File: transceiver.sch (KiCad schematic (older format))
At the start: 44 parts, among them U3 CC1200, Y1 40 Mhz crystal

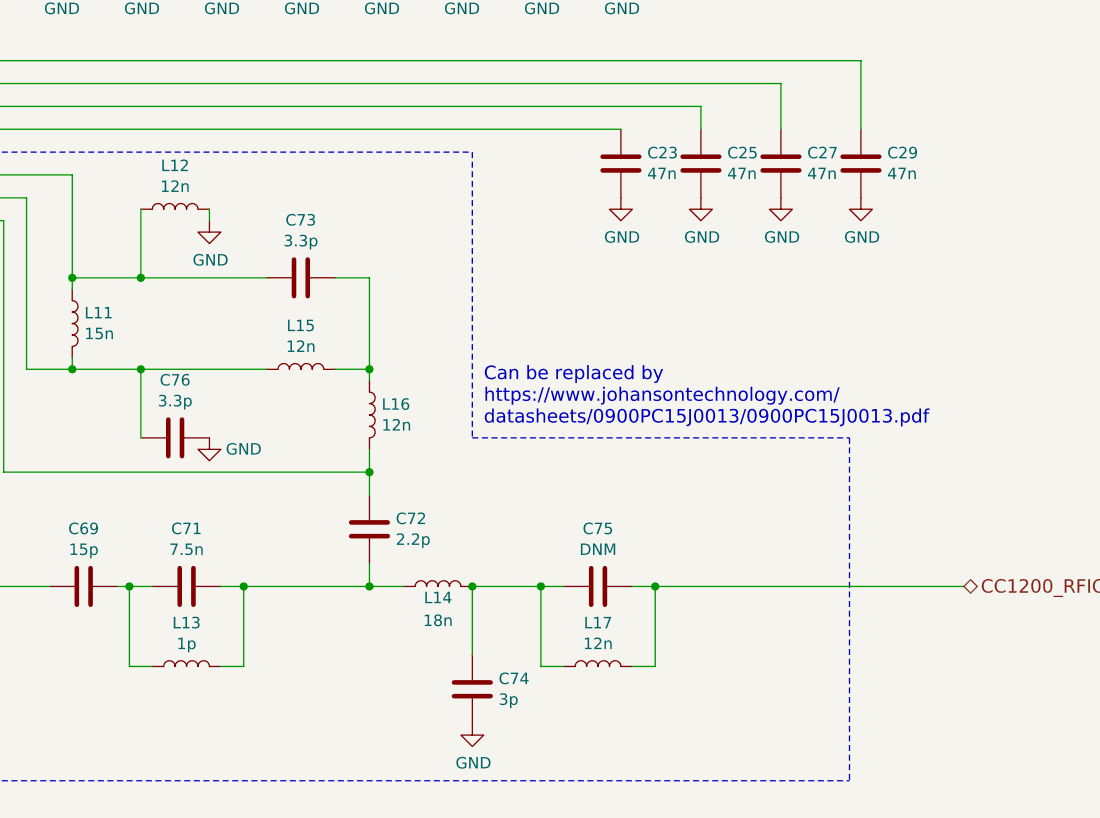
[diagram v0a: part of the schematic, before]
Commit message: Corrected some component values
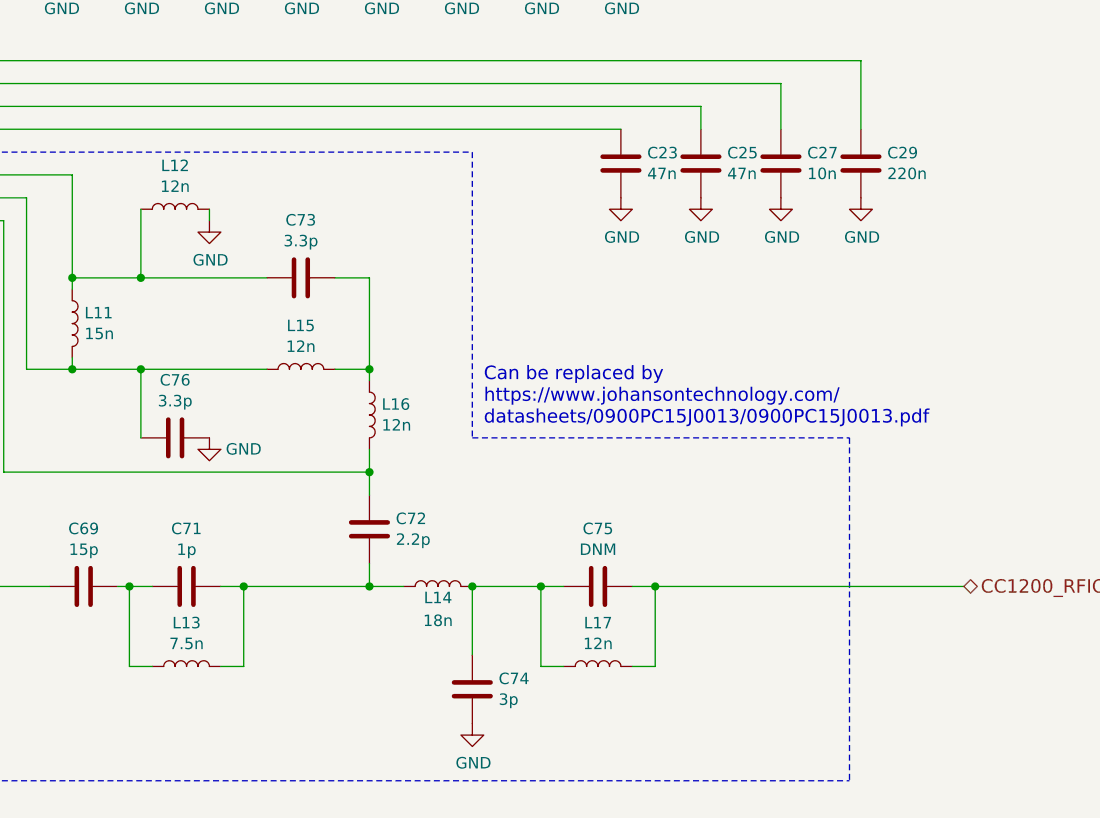
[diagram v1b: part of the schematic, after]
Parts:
- C27: value 47n -> 10n
- C29: value 47n -> 220n
- C71: value 7.5n -> 1p
- L13: value 1p -> 7.5n
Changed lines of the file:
@@
 P 6600 5300
 F 0 "C71" V 6348 5300 50  0000 C CNN
-F 1 "7.5n" V 6439 5300 50  0000 C CNN
+F 1 "1p" V 6439 5300 50  0000 C CNN
 F 2 "" H 6638 5150 50  0001 C CNN
 F 3 "~" H 6600 5300 50  0001 C CNN
@@
 P 6600 5650
 F 0 "L13" V 6790 5650 50  0000 C CNN
-F 1 "1p" V 6699 5650 50  0000 C CNN
+F 1 "7.5n" V 6699 5650 50  0000 C CNN
 F 2 "" H 6600 5650 50  0001 C CNN
 F 3 "~" H 6600 5650 50  0001 C CNN
@@
 P 9200 3450
 F 0 "C27" H 9315 3496 50  0000 L CNN
-F 1 "47n" H 9315 3405 50  0000 L CNN
+F 1 "10n" H 9315 3405 50  0000 L CNN
 F 2 "" H 9238 3300 50  0001 C CNN
 F 3 "~" H 9200 3450 50  0001 C CNN
@@
 P 9550 3450
 F 0 "C29" H 9665 3496 50  0000 L CNN
-F 1 "47n" H 9665 3405 50  0000 L CNN
+F 1 "220n" H 9665 3405 50  0000 L CNN
 F 2 "" H 9588 3300 50  0001 C CNN
 F 3 "~" H 9550 3450 50  0001 C CNN

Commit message: Added MCU config pins
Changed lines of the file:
@@
 $Descr A4 11693 8268
 encoding utf-8
-Sheet 6 6
+Sheet 5 6
 Title ""
 Date ""
@@
 Wire Wire Line
 	1750 2900 2400 2900
-Wire Wire Line
-	5400 2000 5400 1900
 $Comp
 L Device:C C60
@@
 Wire Wire Line
 	5550 5100 5550 5300
+Wire Wire Line
+	5400 1900 5400 2000
 $EndSCHEMATC

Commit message: Changes to PA layout
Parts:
- C19, C20, C21, C22, C23, C24, C25, C26, C27, C28, C29, C30, C31, C32, C57, C58, C59, C60, C61, C62, C66, C67, C68, C69, C71, C72, C73, C74, C75, C76: footprint (none) -> Capacitor_SMD:C_0603_1608Metric
- L10, L11, L12, L13, L14, L15, L16, L17: footprint (none) -> Inductor_SMD:L_0603_1608Metric
- R13, R6: footprint (none) -> Resistor_SMD:R_0603_1608Metric
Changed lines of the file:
@@
 $Descr A4 11693 8268
 encoding utf-8
-Sheet 5 6
+Sheet 4 6
 Title ""
 Date ""
@@
 F 0 "C23" H 8615 3496 50  0000 L CNN
 F 1 "47n" H 8615 3405 50  0000 L CNN
-F 2 "" H 8538 3300 50  0001 C CNN
+F 2 "Capacitor_SMD:C_0603_1608Metric" H 8538 3300 50  0001 C CNN
 F 3 "~" H 8500 3450 50  0001 C CNN
 	1    8500 3450
@@
 F 0 "R6" H 3080 3604 50  0000 R CNN
 F 1 "56k" H 3080 3695 50  0000 R CNN
-F 2 "" V 3080 3650 50  0001 C CNN
+F 2 "Resistor_SMD:R_0603_1608Metric" V 3080 3650 50  0001 C CNN
 F 3 "~" H 3150 3650 50  0001 C CNN
 	1    3150 3650
@@
 F 0 "C59" H 2915 3696 50  0000 L CNN
 F 1 "DNM" H 2915 3605 50  0000 L CNN
-F 2 "" H 2838 3500 50  0001 C CNN
+F 2 "Capacitor_SMD:C_0603_1608Metric" H 2838 3500 50  0001 C CNN
 F 3 "~" H 2800 3650 50  0001 C CNN
 	1    2800 3650
@@
 F 0 "C58" H 2515 3696 50  0000 L CNN
 F 1 "15p" H 2515 3605 50  0000 L CNN
-F 2 "" H 2438 3500 50  0001 C CNN
+F 2 "Capacitor_SMD:C_0603_1608Metric" H 2438 3500 50  0001 C CNN
 F 3 "~" H 2400 3650 50  0001 C CNN
 	1    2400 3650
@@
 F 0 "C57" H 2115 3696 50  0000 L CNN
 F 1 "15p" H 2115 3605 50  0000 L CNN
-F 2 "" H 2038 3500 50  0001 C CNN
+F 2 "Capacitor_SMD:C_0603_1608Metric" H 2038 3500 50  0001 C CNN
 F 3 "~" H 2000 3650 50  0001 C CNN
 	1    2000 3650
@@
 F 0 "C60" H 2165 1446 50  0000 L CNN
 F 1 "100n" H 2165 1355 50  0000 L CNN
-F 2 "" H 2088 1250 50  0001 C CNN
+F 2 "Capacitor_SMD:C_0603_1608Metric" H 2088 1250 50  0001 C CNN
 F 3 "~" H 2050 1400 50  0001 C CNN
 	1    2050 1400
@@
 F 0 "C62" H 3865 1446 50  0000 L CNN
 F 1 "2.2u" H 3865 1355 50  0000 L CNN
-F 2 "" H 3788 1250 50  0001 C CNN
+F 2 "Capacitor_SMD:C_0603_1608Metric" H 3788 1250 50  0001 C CNN
 F 3 "~" H 3750 1400 50  0001 C CNN
 	1    3750 1400
@@
 F 0 "R13" H 5220 5346 50  0000 L CNN
 F 1 "10" H 5220 5255 50  0000 L CNN
-F 2 "" V 5080 5300 50  0001 C CNN
+F 2 "Resistor_SMD:R_0603_1608Metric" V 5080 5300 50  0001 C CNN
 F 3 "~" H 5150 5300 50  0001 C CNN
 	1    5150 5300
@@
 F 0 "C67" H 4915 5346 50  0000 L CNN
 F 1 "33p" H 4915 5255 50  0000 L CNN
-F 2 "" H 4838 5150 50  0001 C CNN
+F 2 "Capacitor_SMD:C_0603_1608Metric" H 4838 5150 50  0001 C CNN
 F 3 "~" H 4800 5300 50  0001 C CNN
 	1    4800 5300
@@
 F 0 "C66" H 5265 5796 50  0000 L CNN
 F 1 "10n" H 5265 5705 50  0000 L CNN
-F 2 "" H 5188 5600 50  0001 C CNN
+F 2 "Capacitor_SMD:C_0603_1608Metric" H 5188 5600 50  0001 C CNN
 F 3 "~" H 5150 5750 50  0001 C CNN
 	1    5150 5750
@@
 F 0 "C68" H 4915 5796 50  0000 L CNN
 F 1 "100p" H 4915 5705 50  0000 L CNN
-F 2 "" H 4838 5600 50  0001 C CNN
+F 2 "Capacitor_SMD:C_0603_1608Metric" H 4838 5600 50  0001 C CNN
 F 3 "~" H 4800 5750 50  0001 C CNN
 	1    4800 5750
@@
 F 0 "C69" V 5898 5300 50  0000 C CNN
 F 1 "15p" V 5989 5300 50  0000 C CNN
-F 2 "" H 6188 5150 50  0001 C CNN
+F 2 "Capacitor_SMD:C_0603_1608Metric" H 6188 5150 50  0001 C CNN
 F 3 "~" H 6150 5300 50  0001 C CNN
 	1    6150 5300
@@
 F 0 "C71" V 6348 5300 50  0000 C CNN
 F 1 "1p" V 6439 5300 50  0000 C CNN
-F 2 "" H 6638 5150 50  0001 C CNN
+F 2 "Capacitor_SMD:C_0603_1608Metric" H 6638 5150 50  0001 C CNN
 F 3 "~" H 6600 5300 50  0001 C CNN
 	1    6600 5300
@@
 F 0 "L13" V 6790 5650 50  0000 C CNN
 F 1 "7.5n" V 6699 5650 50  0000 C CNN
-F 2 "" H 6600 5650 50  0001 C CNN
+F 2 "Inductor_SMD:L_0603_1608Metric" H 6600 5650 50  0001 C CNN
 F 3 "~" H 6600 5650 50  0001 C CNN
 	1    6600 5650
@@
 F 0 "C75" V 8148 5300 50  0000 C CNN
 F 1 "DNM" V 8239 5300 50  0000 C CNN
-F 2 "" H 8438 5150 50  0001 C CNN
+F 2 "Capacitor_SMD:C_0603_1608Metric" H 8438 5150 50  0001 C CNN
 F 3 "~" H 8400 5300 50  0001 C CNN
 	1    8400 5300
@@
 F 0 "L17" V 8590 5650 50  0000 C CNN
 F 1 "12n" V 8499 5650 50  0000 C CNN
-F 2 "" H 8400 5650 50  0001 C CNN
+F 2 "Inductor_SMD:L_0603_1608Metric" H 8400 5650 50  0001 C CNN
 F 3 "~" H 8400 5650 50  0001 C CNN
 	1    8400 5650
@@
 F 0 "C74" H 7965 5796 50  0000 L CNN
 F 1 "3p" H 7965 5705 50  0000 L CNN
-F 2 "" H 7888 5600 50  0001 C CNN
+F 2 "Capacitor_SMD:C_0603_1608Metric" H 7888 5600 50  0001 C CNN
 F 3 "~" H 7850 5750 50  0001 C CNN
 	1    7850 5750
@@
 F 0 "L14" V 7650 5300 50  0000 C CNN
 F 1 "18n" V 7550 5300 50  0000 C CNN
-F 2 "" H 7700 5300 50  0001 C CNN
+F 2 "Inductor_SMD:L_0603_1608Metric" H 7700 5300 50  0001 C CNN
 F 3 "~" H 7700 5300 50  0001 C CNN
 	1    7700 5300
@@
 F 0 "L15" V 7290 4350 50  0000 C CNN
 F 1 "12n" V 7199 4350 50  0000 C CNN
-F 2 "" H 7100 4350 50  0001 C CNN
+F 2 "Inductor_SMD:L_0603_1608Metric" H 7100 4350 50  0001 C CNN
 F 3 "~" H 7100 4350 50  0001 C CNN
 	1    7100 4350
@@
 F 0 "L16" H 7453 4596 50  0000 L CNN
 F 1 "12n" H 7453 4505 50  0000 L CNN
-F 2 "" H 7400 4550 50  0001 C CNN
+F 2 "Inductor_SMD:L_0603_1608Metric" H 7400 4550 50  0001 C CNN
 F 3 "~" H 7400 4550 50  0001 C CNN
 	1    7400 4550
@@
 F 0 "C73" V 6848 3950 50  0000 C CNN
 F 1 "3.3p" V 6939 3950 50  0000 C CNN
-F 2 "" H 7138 3800 50  0001 C CNN
+F 2 "Capacitor_SMD:C_0603_1608Metric" H 7138 3800 50  0001 C CNN
 F 3 "~" H 7100 3950 50  0001 C CNN
 	1    7100 3950
@@
 F 0 "L12" V 6740 3650 50  0000 C CNN
 F 1 "12n" V 6649 3650 50  0000 C CNN
-F 2 "" H 6550 3650 50  0001 C CNN
+F 2 "Inductor_SMD:L_0603_1608Metric" H 6550 3650 50  0001 C CNN
 F 3 "~" H 6550 3650 50  0001 C CNN
 	1    6550 3650
@@
 F 0 "C76" V 6298 4650 50  0000 C CNN
 F 1 "3.3p" V 6389 4650 50  0000 C CNN
-F 2 "" H 6588 4500 50  0001 C CNN
+F 2 "Capacitor_SMD:C_0603_1608Metric" H 6588 4500 50  0001 C CNN
 F 3 "~" H 6550 4650 50  0001 C CNN
 	1    6550 4650
@@
 F 0 "C72" H 7515 5096 50  0000 L CNN
 F 1 "2.2p" H 7515 5005 50  0000 L CNN
-F 2 "" H 7438 4900 50  0001 C CNN
+F 2 "Capacitor_SMD:C_0603_1608Metric" H 7438 4900 50  0001 C CNN
 F 3 "~" H 7400 5050 50  0001 C CNN
 	1    7400 5050
@@
 F 0 "L10" V 5540 5100 50  0000 C CNN
 F 1 "10n" V 5449 5100 50  0000 C CNN
-F 2 "" H 5350 5100 50  0001 C CNN
+F 2 "Inductor_SMD:L_0603_1608Metric" H 5350 5100 50  0001 C CNN
 F 3 "~" H 5350 5100 50  0001 C CNN
 	1    5350 5100
@@
 F 0 "C25" H 8965 3496 50  0000 L CNN
 F 1 "47n" H 8965 3405 50  0000 L CNN
-F 2 "" H 8888 3300 50  0001 C CNN
+F 2 "Capacitor_SMD:C_0603_1608Metric" H 8888 3300 50  0001 C CNN
 F 3 "~" H 8850 3450 50  0001 C CNN
 	1    8850 3450
@@
 F 0 "C27" H 9315 3496 50  0000 L CNN
 F 1 "10n" H 9315 3405 50  0000 L CNN
-F 2 "" H 9238 3300 50  0001 C CNN
+F 2 "Capacitor_SMD:C_0603_1608Metric" H 9238 3300 50  0001 C CNN
 F 3 "~" H 9200 3450 50  0001 C CNN
 	1    9200 3450
@@
 F 0 "C29" H 9665 3496 50  0000 L CNN
 F 1 "220n" H 9665 3405 50  0000 L CNN
-F 2 "" H 9588 3300 50  0001 C CNN
+F 2 "Capacitor_SMD:C_0603_1608Metric" H 9588 3300 50  0001 C CNN
 F 3 "~" H 9550 3450 50  0001 C CNN
 	1    9550 3450
@@
 F 0 "C20" H 5815 2496 50  0000 L CNN
 F 1 "47n" H 5815 2405 50  0000 L CNN
-F 2 "" H 5738 2300 50  0001 C CNN
+F 2 "Capacitor_SMD:C_0603_1608Metric" H 5738 2300 50  0001 C CNN
 F 3 "~" H 5700 2450 50  0001 C CNN
 	1    5700 2450
@@
 F 0 "C21" H 6165 2496 50  0000 L CNN
 F 1 "47n" H 6165 2405 50  0000 L CNN
-F 2 "" H 6088 2300 50  0001 C CNN
+F 2 "Capacitor_SMD:C_0603_1608Metric" H 6088 2300 50  0001 C CNN
 F 3 "~" H 6050 2450 50  0001 C CNN
 	1    6050 2450
@@
 F 0 "C22" H 6515 2496 50  0000 L CNN
 F 1 "47n" H 6515 2405 50  0000 L CNN
-F 2 "" H 6438 2300 50  0001 C CNN
+F 2 "Capacitor_SMD:C_0603_1608Metric" H 6438 2300 50  0001 C CNN
 F 3 "~" H 6400 2450 50  0001 C CNN
 	1    6400 2450
@@
 F 0 "C24" H 6865 2496 50  0000 L CNN
 F 1 "47n" H 6865 2405 50  0000 L CNN
-F 2 "" H 6788 2300 50  0001 C CNN
+F 2 "Capacitor_SMD:C_0603_1608Metric" H 6788 2300 50  0001 C CNN
 F 3 "~" H 6750 2450 50  0001 C CNN
 	1    6750 2450
@@
 F 0 "C26" H 7215 2496 50  0000 L CNN
 F 1 "47n" H 7215 2405 50  0000 L CNN
-F 2 "" H 7138 2300 50  0001 C CNN
+F 2 "Capacitor_SMD:C_0603_1608Metric" H 7138 2300 50  0001 C CNN
 F 3 "~" H 7100 2450 50  0001 C CNN
 	1    7100 2450
@@
 F 0 "C28" H 7565 2496 50  0000 L CNN
 F 1 "47n" H 7565 2405 50  0000 L CNN
-F 2 "" H 7488 2300 50  0001 C CNN
+F 2 "Capacitor_SMD:C_0603_1608Metric" H 7488 2300 50  0001 C CNN
 F 3 "~" H 7450 2450 50  0001 C CNN
 	1    7450 2450
@@
 F 0 "C30" H 7915 2496 50  0000 L CNN
 F 1 "47n" H 7915 2405 50  0000 L CNN
-F 2 "" H 7838 2300 50  0001 C CNN
+F 2 "Capacitor_SMD:C_0603_1608Metric" H 7838 2300 50  0001 C CNN
 F 3 "~" H 7800 2450 50  0001 C CNN
 	1    7800 2450
@@
 F 0 "C31" H 8265 2496 50  0000 L CNN
 F 1 "47n" H 8265 2405 50  0000 L CNN
-F 2 "" H 8188 2300 50  0001 C CNN
+F 2 "Capacitor_SMD:C_0603_1608Metric" H 8188 2300 50  0001 C CNN
 F 3 "~" H 8150 2450 50  0001 C CNN
 	1    8150 2450
@@
 F 0 "C32" H 8615 2496 50  0000 L CNN
 F 1 "47n" H 8615 2405 50  0000 L CNN
-F 2 "" H 8538 2300 50  0001 C CNN
+F 2 "Capacitor_SMD:C_0603_1608Metric" H 8538 2300 50  0001 C CNN
 F 3 "~" H 8500 2450 50  0001 C CNN
 	1    8500 2450
@@
 F 0 "C61" H 3165 1446 50  0000 L CNN
 F 1 "DNM" H 3165 1355 50  0000 L CNN
-F 2 "" H 3088 1250 50  0001 C CNN
+F 2 "Capacitor_SMD:C_0603_1608Metric" H 3088 1250 50  0001 C CNN
 F 3 "~" H 3050 1400 50  0001 C CNN
 	1    3050 1400
@@
 F 0 "C19" H 3565 3696 50  0000 L CNN
 F 1 "1.5n" H 3565 3605 50  0000 L CNN
-F 2 "" H 3488 3500 50  0001 C CNN
+F 2 "Capacitor_SMD:C_0603_1608Metric" H 3488 3500 50  0001 C CNN
 F 3 "~" H 3450 3650 50  0001 C CNN
 	1    3450 3650
@@
 F 0 "L11" H 6153 4196 50  0000 L CNN
 F 1 "15n" H 6153 4105 50  0000 L CNN
-F 2 "" H 6100 4150 50  0001 C CNN
+F 2 "Inductor_SMD:L_0603_1608Metric" H 6100 4150 50  0001 C CNN
 F 3 "~" H 6100 4150 50  0001 C CNN
 	1    6100 4150

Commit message: Lots of work on routing and pcb layout
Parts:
- removed Y1: 40 Mhz crystal, symbol Device:Crystal_GND23
- added Y1: Crystal_GND24, KTHFS:ndk_08142018_NX3225SA, symbol Device:Crystal_GND24
- C19: value 1.5n -> 1.8n
- C71: value 1p -> DNM
- C73, C76: value 3.3p -> 3p
- FB2: footprint (none) -> Capacitor_SMD:C_0805_2012Metric
- L10: value 10n -> 8.2n
- L13: value 7.5n -> 12n
- TP2: footprint (none) -> TestPoint:TestPoint_Pad_2.0x2.0mm
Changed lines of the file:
@@
 	1    0    0    -1
-$EndComp
-$Comp
-L Device:Crystal_GND23 Y1
-U 1 1 601A879D
-P 1750 3050
-F 0 "Y1" V 1400 3000 50  0000 L CNN
-F 1 "40 Mhz crystal" V 1500 2800 50  0000 L CNN
-F 2 "" H 1750 3050 50  0001 C CNN
-F 3 "~" H 1750 3050 50  0001 C CNN
-	1    1750 3050
-	0    1    1    0
 $EndComp
 Wire Wire Line
@@
 Wire Wire Line
 	2000 3800 2000 4100
-Wire Wire Line
-	1550 3250 1550 3050
-Wire Wire Line
-	1950 3050 1950 3250
 Wire Wire Line
 	1750 3200 2000 3200
@@
 F 0 "FB2" V 2426 1150 50  0000 C CNN
 F 1 "Ferrite_Bead" V 2517 1150 50  0000 C CNN
-F 2 "" V 2630 1150 50  0001 C CNN
+F 2 "Capacitor_SMD:C_0805_2012Metric" V 2630 1150 50  0001 C CNN
 F 3 "~" H 2700 1150 50  0001 C CNN
 	1    2700 1150
@@
 P 6600 5300
 F 0 "C71" V 6348 5300 50  0000 C CNN
-F 1 "1p" V 6439 5300 50  0000 C CNN
+F 1 "DNM" V 6439 5300 50  0000 C CNN
 F 2 "Capacitor_SMD:C_0603_1608Metric" H 6638 5150 50  0001 C CNN
 F 3 "~" H 6600 5300 50  0001 C CNN
@@
 P 6600 5650
 F 0 "L13" V 6790 5650 50  0000 C CNN
-F 1 "7.5n" V 6699 5650 50  0000 C CNN
+F 1 "12n" V 6699 5650 50  0000 C CNN
 F 2 "Inductor_SMD:L_0603_1608Metric" H 6600 5650 50  0001 C CNN
 F 3 "~" H 6600 5650 50  0001 C CNN
@@
 P 7100 3950
 F 0 "C73" V 6848 3950 50  0000 C CNN
-F 1 "3.3p" V 6939 3950 50  0000 C CNN
+F 1 "3p" V 6939 3950 50  0000 C CNN
 F 2 "Capacitor_SMD:C_0603_1608Metric" H 7138 3800 50  0001 C CNN
 F 3 "~" H 7100 3950 50  0001 C CNN
@@
 P 6550 4650
 F 0 "C76" V 6298 4650 50  0000 C CNN
-F 1 "3.3p" V 6389 4650 50  0000 C CNN
+F 1 "3p" V 6389 4650 50  0000 C CNN
 F 2 "Capacitor_SMD:C_0603_1608Metric" H 6588 4500 50  0001 C CNN
 F 3 "~" H 6550 4650 50  0001 C CNN
@@
 	3900 3200 3900 3900
 Connection ~ 3900 3900
-Connection ~ 1550 3250
 Connection ~ 2400 2900
 Connection ~ 2800 2900
 Wire Wire Line
 	2800 2900 3350 2900
-Wire Wire Line
-	1550 3250 1950 3250
 Wire Wire Line
 	2400 2900 2800 2900
@@
 P 5350 5100
 F 0 "L10" V 5540 5100 50  0000 C CNN
-F 1 "10n" V 5449 5100 50  0000 C CNN
+F 1 "8.2n" V 5449 5100 50  0000 C CNN
 F 2 "Inductor_SMD:L_0603_1608Metric" H 5350 5100 50  0001 C CNN
 F 3 "~" H 5350 5100 50  0001 C CNN
@@
 P 3450 3650
 F 0 "C19" H 3565 3696 50  0000 L CNN
-F 1 "1.5n" H 3565 3605 50  0000 L CNN
+F 1 "1.8n" H 3565 3605 50  0000 L CNN
 F 2 "Capacitor_SMD:C_0603_1608Metric" H 3488 3500 50  0001 C CNN
 F 3 "~" H 3450 3650 50  0001 C CNN
@@
 	1    0    0    -1
 $EndComp
-Wire Wire Line
-	1550 3250 1550 4100
 Wire Wire Line
 	2050 1150 2550 1150
@@
 F 0 "TP2" V 5629 1338 50  0000 L CNN
 F 1 "VDD_CC1200" V 5720 1338 50  0000 L CNN
-F 2 "" H 5875 1150 50  0001 C CNN
+F 2 "TestPoint:TestPoint_Pad_2.0x2.0mm" H 5875 1150 50  0001 C CNN
 F 3 "~" H 5875 1150 50  0001 C CNN
 	1    5675 1150
@@
 Wire Wire Line
 	5400 1900 5400 2000
+Wire Wire Line
+	1950 3050 1950 3250
+Wire Wire Line
+	1550 3250 1550 4100
+Wire Wire Line
+	1550 3250 1550 3050
+Connection ~ 1550 3250
+Wire Wire Line
+	1550 3250 1950 3250
+$Comp
+L Device:Crystal_GND24 Y1
+U 1 1 602C539E
+P 1750 3050
+F 0 "Y1" H 1944 3096 50  0000 L CNN
+F 1 "Crystal_GND24" V 2100 2800 50  0000 L CNN
+F 2 "KTHFS:ndk_08142018_NX3225SA" H 1750 3050 50  0001 C CNN
+F 3 "~" H 1750 3050 50  0001 C CNN
+	1    1750 3050
+	0    -1   -1   0
+$EndComp
 $EndSCHEMATC
